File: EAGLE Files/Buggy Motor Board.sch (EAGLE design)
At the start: 53 parts, among them CON0 M025MM, CON1 M025MM, IC4 4050D, IC5 LP298XS, U1 MCP2551, X1 MICROSD, X2 5566-24, X3 5566-24, Y2 16MHZ

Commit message: Microfit connector
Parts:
- removed X4, X5, X6, X7: (no value), con-wago-500:W237-4
- added U$10: WM9300, Wetmelon-Connectors:WM9300
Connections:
- net CHAN0: no longer X4-1.KL
- net CHAN1: no longer X4-2.KL
- net CHAN10: no longer X6-3.KL
- net CHAN11: no longer X6-4.KL
- net CHAN12: no longer X7-1.KL
- net CHAN13: no longer X7-2.KL
- net CHAN14: no longer X7-3.KL
- net CHAN15: no longer X7-4.KL
- net CHAN2: no longer X4-3.KL
- net CHAN3: no longer X4-4.KL
- net CHAN4: no longer X5-1.KL
- net CHAN5: no longer X5-2.KL
- net CHAN6: no longer X5-3.KL
- net CHAN7: no longer X5-4.KL
- net CHAN8: no longer X6-1.KL
- net CHAN9: no longer X6-2.KL
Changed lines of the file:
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@@
 <setting verticaltext="up"/>
 </settings>
-<grid distance="0.1" unitdist="inch" unit="inch" style="lines" multiple="1" display="yes" altdistance="0.01" altunitdist="inch" altunit="inch"/>
+<grid distance="0.1" unitdist="inch" unit="inch" style="lines" multiple="1" display="no" altdistance="0.01" altunitdist="inch" altunit="inch"/>
 <layers>
 <layer number="1" name="Top" color="4" fill="1" visible="no" active="no"/>
@@
 <part name="C4" library="rcl" deviceset="C-US" device="C1210K"/>
 <part name="C5" library="rcl" deviceset="C-US" device="C1210K"/>
-<part name="X4" library="con-wago-500" deviceset="W237-4" device=""/>
-<part name="X5" library="con-wago-500" deviceset="W237-4" device=""/>
-<part name="X6" library="con-wago-500" deviceset="W237-4" device=""/>
-<part name="X7" library="con-wago-500" deviceset="W237-4" device=""/>
+<part name="U$10" library="Wetmelon-Connectors" deviceset="WM9300" device=""/>
 </parts>
 <sheets>
@@
 <instance part="C4" gate="G$1" x="292.1" y="106.68"/>
 <instance part="C5" gate="G$1" x="231.14" y="106.68"/>
-<instance part="X4" gate="-1" x="177.8" y="12.7" rot="R90"/>
-<instance part="X4" gate="-2" x="182.88" y="12.7" rot="R90"/>
-<instance part="X4" gate="-3" x="187.96" y="12.7" rot="R90"/>
-<instance part="X4" gate="-4" x="193.04" y="12.7" rot="R90"/>
-<instance part="X5" gate="-1" x="198.12" y="12.7" rot="R90"/>
-<instance part="X5" gate="-2" x="203.2" y="12.7" rot="R90"/>
-<instance part="X5" gate="-3" x="208.28" y="12.7" rot="R90"/>
-<instance part="X5" gate="-4" x="213.36" y="12.7" rot="R90"/>
-<instance part="X6" gate="-1" x="218.44" y="12.7" rot="R90"/>
-<instance part="X6" gate="-2" x="223.52" y="12.7" rot="R90"/>
-<instance part="X6" gate="-3" x="228.6" y="12.7" rot="R90"/>
-<instance part="X6" gate="-4" x="233.68" y="12.7" rot="R90"/>
-<instance part="X7" gate="-1" x="238.76" y="12.7" rot="R90"/>
-<instance part="X7" gate="-2" x="243.84" y="12.7" rot="R90"/>
-<instance part="X7" gate="-3" x="248.92" y="12.7" rot="R90"/>
-<instance part="X7" gate="-4" x="254" y="12.7" rot="R90"/>
+<instance part="U$10" gate="G$1" x="187.96" y="55.88"/>
 </instances>
 <busses>
@@
 <segment>
 <wire x1="165.1" y1="78.74" x2="165.1" y2="38.1" width="0.762" layer="92"/>
-<wire x1="165.1" y1="38.1" x2="170.18" y2="33.02" width="0.762" layer="92"/>
-<wire x1="170.18" y1="33.02" x2="254" y2="33.02" width="0.762" layer="92"/>
 </segment>
 </bus>
@@
 <label x="154.94" y="78.74" size="1.778" layer="95"/>
 </segment>
-<segment>
-<pinref part="X4" gate="-1" pin="KL"/>
-<wire x1="175.26" y1="33.02" x2="177.8" y2="30.48" width="0.1524" layer="91"/>
-<wire x1="177.8" y1="30.48" x2="177.8" y2="17.78" width="0.1524" layer="91"/>
-<label x="177.8" y="20.32" size="1.778" layer="95" rot="R90"/>
-</segment>
 </net>
 <net name="CHAN1" class="0">
@@
 <wire x1="152.4" y1="76.2" x2="165.1" y2="76.2" width="0.1524" layer="91"/>
 </segment>
-<segment>
-<pinref part="X4" gate="-2" pin="KL"/>
-<wire x1="180.34" y1="33.02" x2="182.88" y2="30.48" width="0.1524" layer="91"/>
-<wire x1="182.88" y1="30.48" x2="182.88" y2="17.78" width="0.1524" layer="91"/>
-<label x="182.88" y="20.32" size="1.778" layer="95" rot="R90"/>
-</segment>
 </net>
 <net name="CHAN2" class="0">
@@
 <wire x1="152.4" y1="73.66" x2="165.1" y2="73.66" width="0.1524" layer="91"/>
 </segment>
-<segment>
-<pinref part="X4" gate="-3" pin="KL"/>
-<wire x1="185.42" y1="33.02" x2="187.96" y2="30.48" width="0.1524" layer="91"/>
-<wire x1="187.96" y1="30.48" x2="187.96" y2="17.78" width="0.1524" layer="91"/>
-<label x="187.96" y="20.32" size="1.778" layer="95" rot="R90"/>
-</segment>
 </net>
 <net name="CHAN3" class="0">
@@
 <wire x1="152.4" y1="71.12" x2="165.1" y2="71.12" width="0.1524" layer="91"/>
 </segment>
-<segment>
-<pinref part="X4" gate="-4" pin="KL"/>
-<wire x1="190.5" y1="33.02" x2="193.04" y2="30.48" width="0.1524" layer="91"/>
-<wire x1="193.04" y1="30.48" x2="193.04" y2="17.78" width="0.1524" layer="91"/>
-<label x="193.04" y="20.32" size="1.778" layer="95" rot="R90"/>
-</segment>
 </net>
 <net name="CHAN4" class="0">
@@
 <wire x1="152.4" y1="68.58" x2="165.1" y2="68.58" width="0.1524" layer="91"/>
 </segment>
-<segment>
-<pinref part="X5" gate="-1" pin="KL"/>
-<wire x1="195.58" y1="33.02" x2="198.12" y2="30.48" width="0.1524" layer="91"/>
-<wire x1="198.12" y1="30.48" x2="198.12" y2="17.78" width="0.1524" layer="91"/>
-<label x="198.12" y="20.32" size="1.778" layer="95" rot="R90"/>
-</segment>
 </net>
 <net name="CHAN5" class="0">
@@
 <wire x1="152.4" y1="66.04" x2="165.1" y2="66.04" width="0.1524" layer="91"/>
 </segment>
-<segment>
-<pinref part="X5" gate="-2" pin="KL"/>
-<wire x1="200.66" y1="33.02" x2="203.2" y2="30.48" width="0.1524" layer="91"/>
-<wire x1="203.2" y1="30.48" x2="203.2" y2="17.78" width="0.1524" layer="91"/>
-<label x="203.2" y="20.32" size="1.778" layer="95" rot="R90"/>
-</segment>
 </net>
 <net name="CHAN6" class="0">
@@
 <wire x1="152.4" y1="63.5" x2="165.1" y2="63.5" width="0.1524" layer="91"/>
 </segment>
-<segment>
-<pinref part="X5" gate="-3" pin="KL"/>
-<wire x1="205.74" y1="33.02" x2="208.28" y2="30.48" width="0.1524" layer="91"/>
-<wire x1="208.28" y1="30.48" x2="208.28" y2="17.78" width="0.1524" layer="91"/>
-<label x="208.28" y="20.32" size="1.778" layer="95" rot="R90"/>
-</segment>
 </net>
 <net name="CHAN7" class="0">
@@
 <wire x1="152.4" y1="60.96" x2="165.1" y2="60.96" width="0.1524" layer="91"/>
 </segment>
-<segment>
-<pinref part="X5" gate="-4" pin="KL"/>
-<wire x1="210.82" y1="33.02" x2="213.36" y2="30.48" width="0.1524" layer="91"/>
-<wire x1="213.36" y1="30.48" x2="213.36" y2="17.78" width="0.1524" layer="91"/>
-<label x="213.36" y="20.32" size="1.778" layer="95" rot="R90"/>
-</segment>
 </net>
 <net name="CHAN8" class="0">
@@
 <wire x1="152.4" y1="58.42" x2="165.1" y2="58.42" width="0.1524" layer="91"/>
 </segment>
-<segment>
-<pinref part="X6" gate="-1" pin="KL"/>
-<wire x1="215.9" y1="33.02" x2="218.44" y2="30.48" width="0.1524" layer="91"/>
-<wire x1="218.44" y1="30.48" x2="218.44" y2="17.78" width="0.1524" layer="91"/>
-<label x="218.44" y="20.32" size="1.778" layer="95" rot="R90"/>
-</segment>
 </net>
 <net name="CHAN9" class="0">
@@
 <wire x1="152.4" y1="55.88" x2="165.1" y2="55.88" width="0.1524" layer="91"/>
 </segment>
-<segment>
-<pinref part="X6" gate="-2" pin="KL"/>
-<wire x1="220.98" y1="33.02" x2="223.52" y2="30.48" width="0.1524" layer="91"/>
-<wire x1="223.52" y1="30.48" x2="223.52" y2="17.78" width="0.1524" layer="91"/>
-<label x="223.52" y="20.32" size="1.778" layer="95" rot="R90"/>
-</segment>
 </net>
 <net name="CHAN10" class="0">
@@
 <wire x1="152.4" y1="53.34" x2="165.1" y2="53.34" width="0.1524" layer="91"/>
 </segment>
-<segment>
-<pinref part="X6" gate="-3" pin="KL"/>
-<wire x1="226.06" y1="33.02" x2="228.6" y2="30.48" width="0.1524" layer="91"/>
-<wire x1="228.6" y1="30.48" x2="228.6" y2="17.78" width="0.1524" layer="91"/>
-<label x="228.6" y="20.32" size="1.778" layer="95" rot="R90"/>
-</segment>
 </net>
 <net name="CHAN11" class="0">
@@
 <wire x1="152.4" y1="50.8" x2="165.1" y2="50.8" width="0.1524" layer="91"/>
 </segment>
-<segment>
-<pinref part="X6" gate="-4" pin="KL"/>
-<wire x1="231.14" y1="33.02" x2="233.68" y2="30.48" width="0.1524" layer="91"/>
-<wire x1="233.68" y1="30.48" x2="233.68" y2="17.78" width="0.1524" layer="91"/>
-<label x="233.68" y="20.32" size="1.778" layer="95" rot="R90"/>
-</segment>
 </net>
 <net name="CHAN12" class="0">
@@
 <wire x1="152.4" y1="48.26" x2="165.1" y2="48.26" width="0.1524" layer="91"/>
 </segment>
-<segment>
-<pinref part="X7" gate="-1" pin="KL"/>
-<wire x1="236.22" y1="33.02" x2="238.76" y2="30.48" width="0.1524" layer="91"/>
-<wire x1="238.76" y1="30.48" x2="238.76" y2="17.78" width="0.1524" layer="91"/>
-<label x="238.76" y="20.32" size="1.778" layer="95" rot="R90"/>
-</segment>
 </net>
 <net name="CHAN13" class="0">
@@
 <wire x1="152.4" y1="45.72" x2="165.1" y2="45.72" width="0.1524" layer="91"/>
 </segment>
-<segment>
-<pinref part="X7" gate="-2" pin="KL"/>
-<wire x1="241.3" y1="33.02" x2="243.84" y2="30.48" width="0.1524" layer="91"/>
-<wire x1="243.84" y1="30.48" x2="243.84" y2="17.78" width="0.1524" layer="91"/>
-<label x="243.84" y="20.32" size="1.778" layer="95" rot="R90"/>
-</segment>
 </net>
 <net name="CHAN14" class="0">
@@
 <pinref part="U$8" gate="G$1" pin="CHAN14"/>
 <wire x1="152.4" y1="43.18" x2="165.1" y2="43.18" width="0.1524" layer="91"/>
-</segment>
-<segment>
-<pinref part="X7" gate="-3" pin="KL"/>
-<wire x1="246.38" y1="33.02" x2="248.92" y2="30.48" width="0.1524" layer="91"/>
-<wire x1="248.92" y1="30.48" x2="248.92" y2="17.78" width="0.1524" layer="91"/>
-<label x="248.92" y="20.32" size="1.778" layer="95" rot="R90"/>
 </segment>
 </net>
@@
 <label x="154.94" y="40.64" size="1.778" layer="95"/>
 </segment>
-<segment>
-<pinref part="X7" gate="-4" pin="KL"/>
-<wire x1="251.46" y1="33.02" x2="254" y2="30.48" width="0.1524" layer="91"/>
-<wire x1="254" y1="30.48" x2="254" y2="17.78" width="0.1524" layer="91"/>
-<label x="254" y="20.32" size="1.778" layer="95" rot="R90"/>
-</segment>
-</net>
+</net>

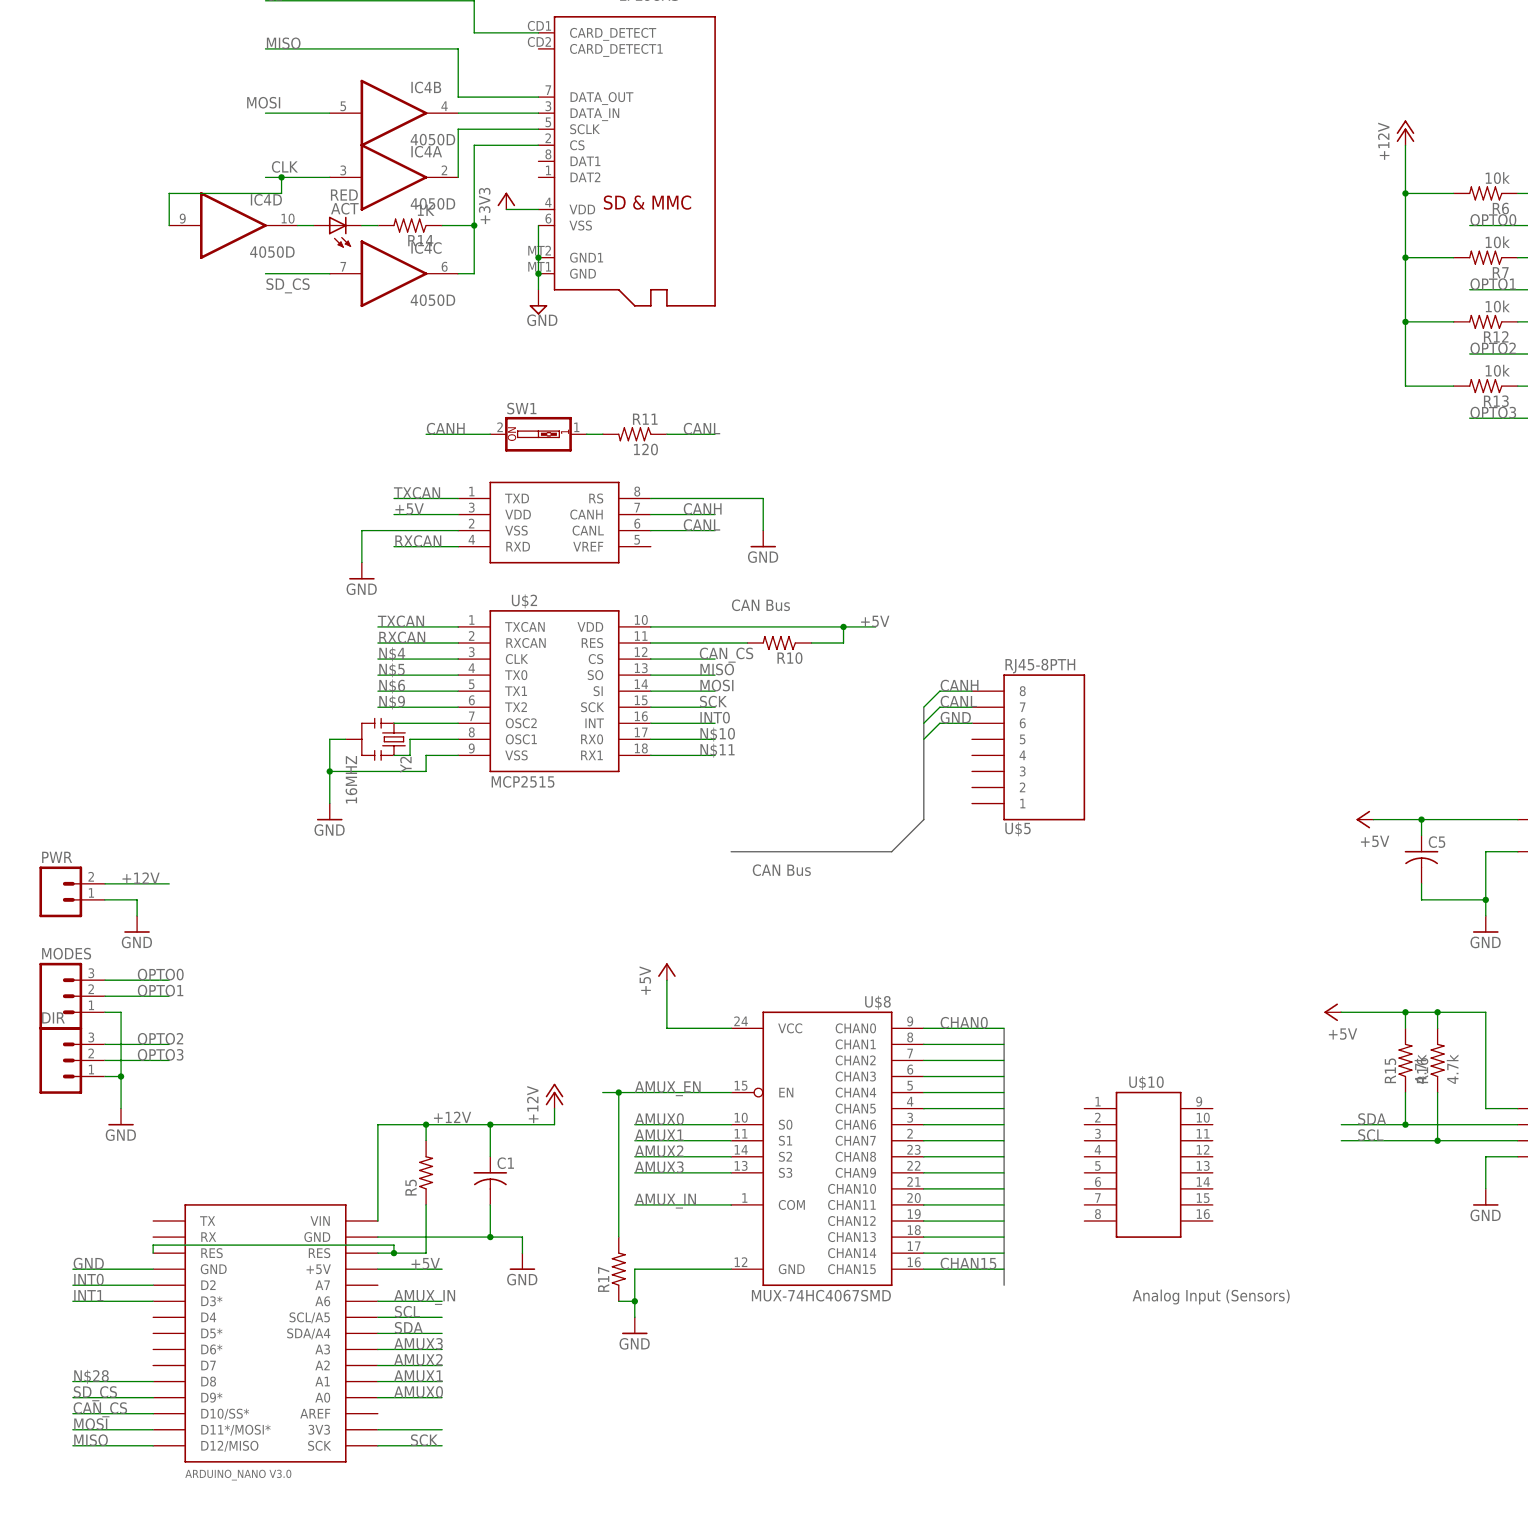
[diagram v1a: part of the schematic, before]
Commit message: 5v Optocoupling
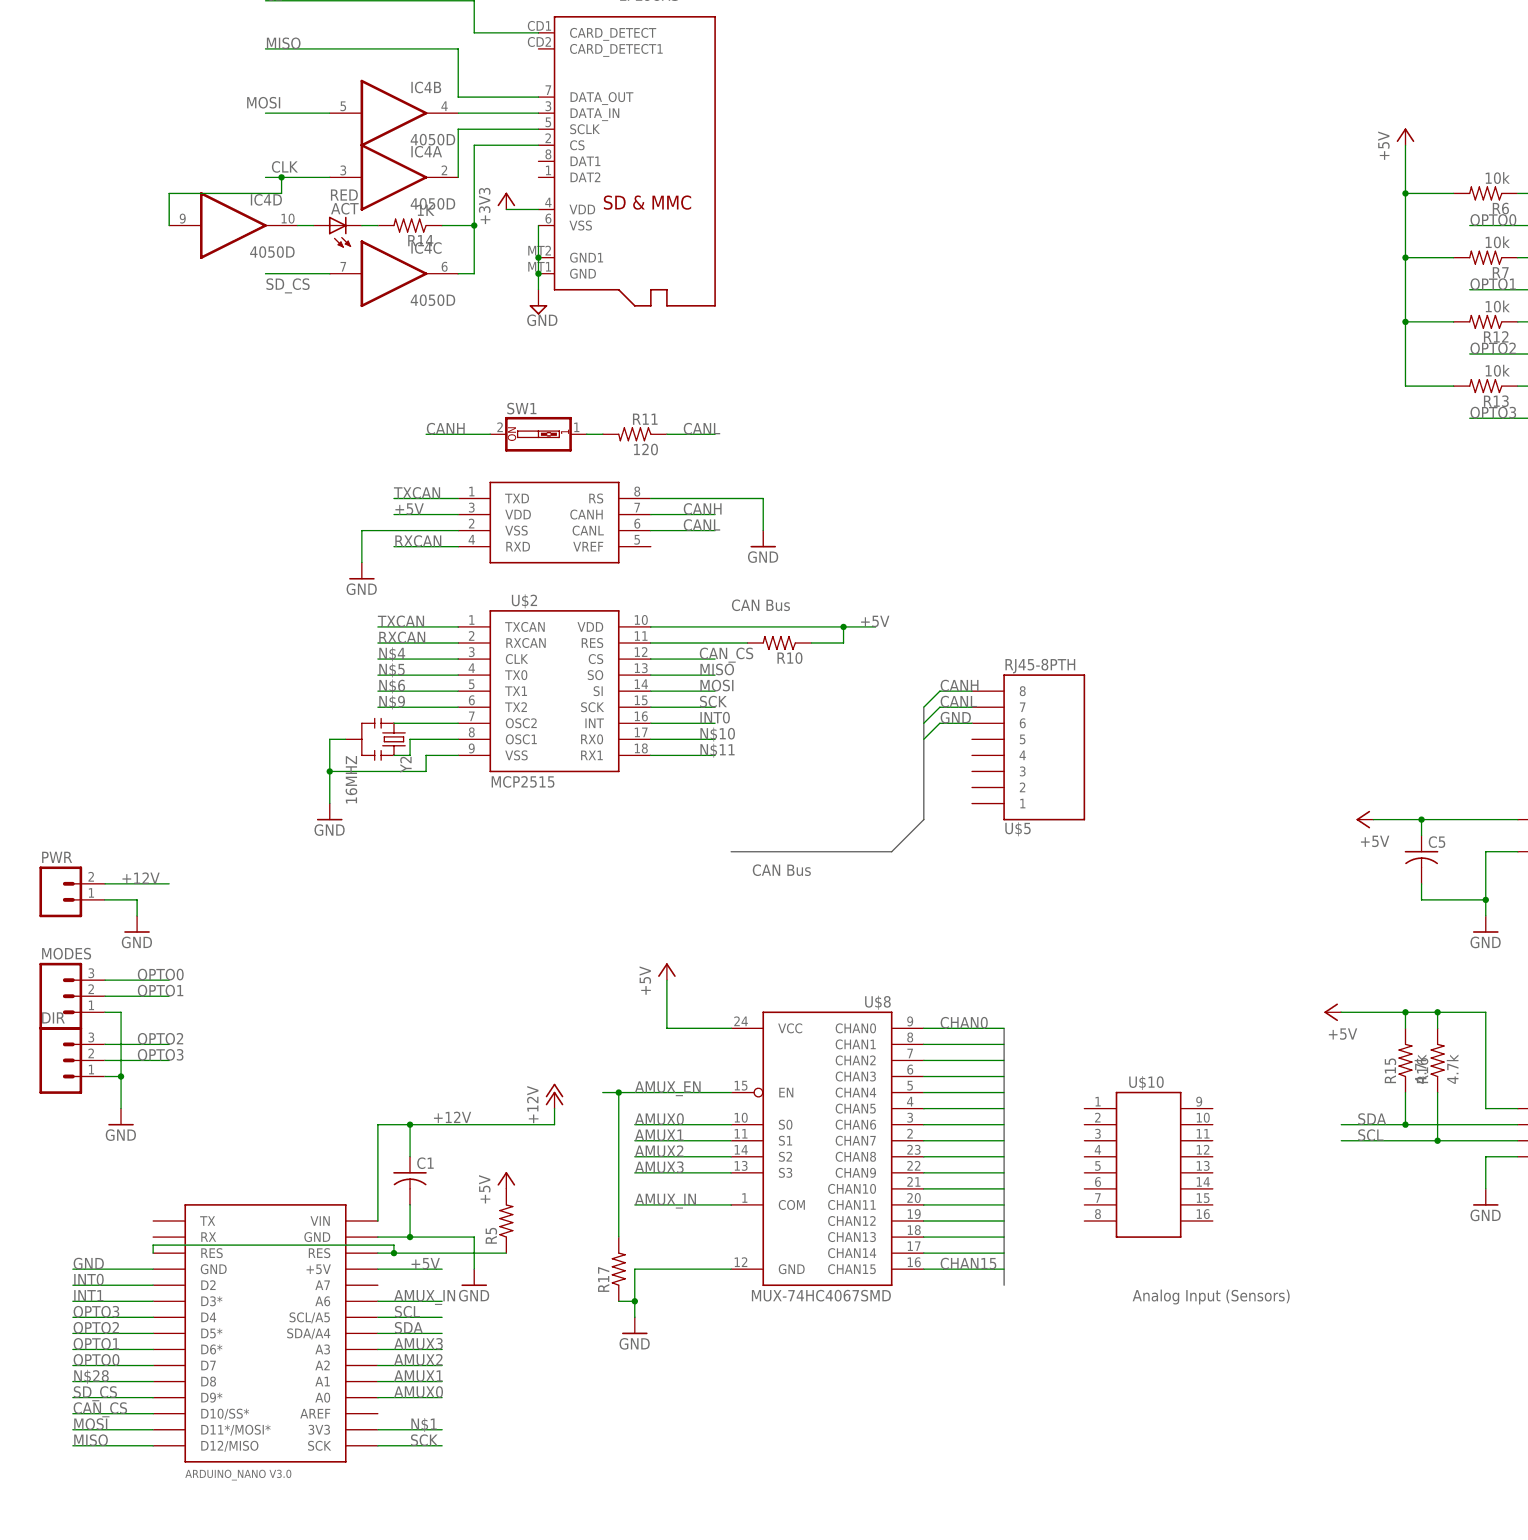
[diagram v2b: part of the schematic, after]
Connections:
- net +12V: no longer R12.2, R13.2, R5.2, R6.2, R7.2
- net +5V: now also R12.2, R13.2, R5.2, R6.2, R7.2
- net OPTO0: now also U$1.D7
- net OPTO1: now also U$1.D6*
- net OPTO2: now also U$1.D5*
- net OPTO3: now also U$1.D4
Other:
- moved on the sheet: C1, R5
